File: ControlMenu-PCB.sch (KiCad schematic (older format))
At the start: 6 parts, among them J1 Conn_01x08, J2 Conn_01x04

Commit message: autosync
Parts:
- 100s1, 10s1, 1s1, Enter1: footprint RobsFoots:PB86-A-FP -> AA-ROB-FULL:PB86-A-FP; symbol robsym1:PB-86A -> AA_ROB:PB-86A-robsym1
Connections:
- wire segments 51 -> 52
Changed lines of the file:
@@
 $EndDescr
 $Comp
-L robsym1:PB-86A 100s1
+L AA_ROB:PB-86A-robsym1 100s1
 U 1 1 5FEB2BAB
 P 4300 3350
 F 0 "100s1" H 4550 4225 50  0000 C CNN
 F 1 "PB-86A" H 4550 4134 50  0000 C CNN
-F 2 "RobsFoots:PB86-A-FP" H 4300 3350 50  0001 C CNN
+F 2 "AA-ROB-FULL:PB86-A-FP" H 4300 3350 50  0001 C CNN
 F 3 "" H 4300 3350 50  0001 C CNN
 	1    4300 3350
@@
 $EndComp
 $Comp
-L robsym1:PB-86A 10s1
+L AA_ROB:PB-86A-robsym1 10s1
 U 1 1 5FEB3BFC
 P 5600 3350
 F 0 "10s1" H 5850 4225 50  0000 C CNN
 F 1 "PB-86A" H 5850 4134 50  0000 C CNN
-F 2 "RobsFoots:PB86-A-FP" H 5600 3350 50  0001 C CNN
+F 2 "AA-ROB-FULL:PB86-A-FP" H 5600 3350 50  0001 C CNN
 F 3 "" H 5600 3350 50  0001 C CNN
 	1    5600 3350
@@
 $EndComp
 $Comp
-L robsym1:PB-86A Enter1
+L AA_ROB:PB-86A-robsym1 Enter1
 U 1 1 5FEB56A3
 P 8300 3350
 F 0 "Enter1" H 8550 4225 50  0000 C CNN
 F 1 "PB-86A" H 8550 4134 50  0000 C CNN
-F 2 "RobsFoots:PB86-A-FP" H 8300 3350 50  0001 C CNN
+F 2 "AA-ROB-FULL:PB86-A-FP" H 8300 3350 50  0001 C CNN
 F 3 "" H 8300 3350 50  0001 C CNN
 	1    8300 3350
@@
 	3400 2850 3400 3400
 Wire Wire Line
-	9450 3400 9450 2600
+	9450 3400 9450 2800
 Wire Wire Line
 	9450 2600 9800 2600
@@
 	4000 2850 3900 2850
 $Comp
-L robsym1:PB-86A 1s1
+L AA_ROB:PB-86A-robsym1 1s1
 U 1 1 5FEB4A66
 P 6900 3350
 F 0 "1s1" H 7150 4225 50  0000 C CNN
 F 1 "PB-86A" H 7150 4134 50  0000 C CNN
-F 2 "RobsFoots:PB86-A-FP" H 6900 3350 50  0001 C CNN
+F 2 "AA-ROB-FULL:PB86-A-FP" H 6900 3350 50  0001 C CNN
 F 3 "" H 6900 3350 50  0001 C CNN
 	1    6900 3350
 	1    0    0    -1
 $EndComp
-Connection ~ 9250 2800
-Wire Wire Line
-	9250 2800 9250 2300
 Wire Wire Line
 	5300 2850 5300 2800
@@
 Wire Wire Line
 	8000 2800 9250 2800
-Wire Wire Line
-	3900 2150 2400 2150
 Connection ~ 5050 2800
 Wire Wire Line
-	3900 2800 3900 2150
-Wire Wire Line
 	3900 2850 3900 2800
-Connection ~ 3900 2800
 Wire Wire Line
 	3900 2800 5050 2800
 Text Notes 7150 6850 0    50   ~ 0
 Version V0.1.1
+Wire Wire Line
+	9250 2150 9250 2300
+Wire Wire Line
+	2400 2150 9250 2150
+Wire Wire Line
+	9250 2800 9450 2800
+Connection ~ 9250 2800
+Connection ~ 9450 2800
+Wire Wire Line
+	9450 2800 9450 2600
 $EndSCHEMATC

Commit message: 5V to Ground Fixes
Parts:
- 100s1, 10s1, 1s1, Enter1: symbol AA_ROB:PB-86A-robsym1 -> AA-ROBSCH:PB-86A
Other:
- note added: "Version V0.1.2"
- note removed: "Version V0.1.1"
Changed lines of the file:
@@
 $EndDescr
 $Comp
-L AA_ROB:PB-86A-robsym1 100s1
+L AA-ROBSCH:PB-86A 100s1
 U 1 1 5FEB2BAB
 P 4300 3350
@@
 $EndComp
 $Comp
-L AA_ROB:PB-86A-robsym1 10s1
+L AA-ROBSCH:PB-86A 10s1
 U 1 1 5FEB3BFC
 P 5600 3350
@@
 $EndComp
 $Comp
-L AA_ROB:PB-86A-robsym1 Enter1
+L AA-ROBSCH:PB-86A Enter1
 U 1 1 5FEB56A3
 P 8300 3350
@@
 Wire Wire Line
 	9250 2850 9250 2800
-Wire Wire Line
-	9250 2300 9800 2300
 $Comp
 L Connector_Generic:Conn_01x04 J2
@@
 Text Notes 9700 2600 0    50   ~ 0
 GND
-Text Label 9250 2450 0    50   ~ 0
-5V
 Text Label 9450 2400 0    50   ~ 0
 SDA
@@
 	4000 2850 3900 2850
 $Comp
-L AA_ROB:PB-86A-robsym1 1s1
+L AA-ROBSCH:PB-86A 1s1
 U 1 1 5FEB4A66
 P 6900 3350
@@
 	3900 2800 5050 2800
 Text Notes 7150 6850 0    50   ~ 0
-Version V0.1.1
-Wire Wire Line
-	9250 2150 9250 2300
-Wire Wire Line
-	2400 2150 9250 2150
+Version V0.1.2
 Wire Wire Line
 	9250 2800 9450 2800
@@
 Wire Wire Line
 	9450 2800 9450 2600
+Wire Wire Line
+	2400 2150 9800 2150
+Wire Wire Line
+	9800 2150 9800 2300
 $EndSCHEMATC

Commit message: RC
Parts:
- 100s1, 10s1, 1s1, Enter1: symbol AA-ROBSCH:PB-86A -> AA-ROBSCH:PB-86A-robsym1
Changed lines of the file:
@@
 $EndDescr
 $Comp
-L AA-ROBSCH:PB-86A 100s1
+L AA-ROBSCH:PB-86A-robsym1 100s1
 U 1 1 5FEB2BAB
 P 4300 3350
@@
 $EndComp
 $Comp
-L AA-ROBSCH:PB-86A 10s1
+L AA-ROBSCH:PB-86A-robsym1 10s1
 U 1 1 5FEB3BFC
 P 5600 3350
@@
 $EndComp
 $Comp
-L AA-ROBSCH:PB-86A Enter1
+L AA-ROBSCH:PB-86A-robsym1 Enter1
 U 1 1 5FEB56A3
 P 8300 3350
@@
 	4000 2850 3900 2850
 $Comp
-L AA-ROBSCH:PB-86A 1s1
+L AA-ROBSCH:PB-86A-robsym1 1s1
 U 1 1 5FEB4A66
 P 6900 3350

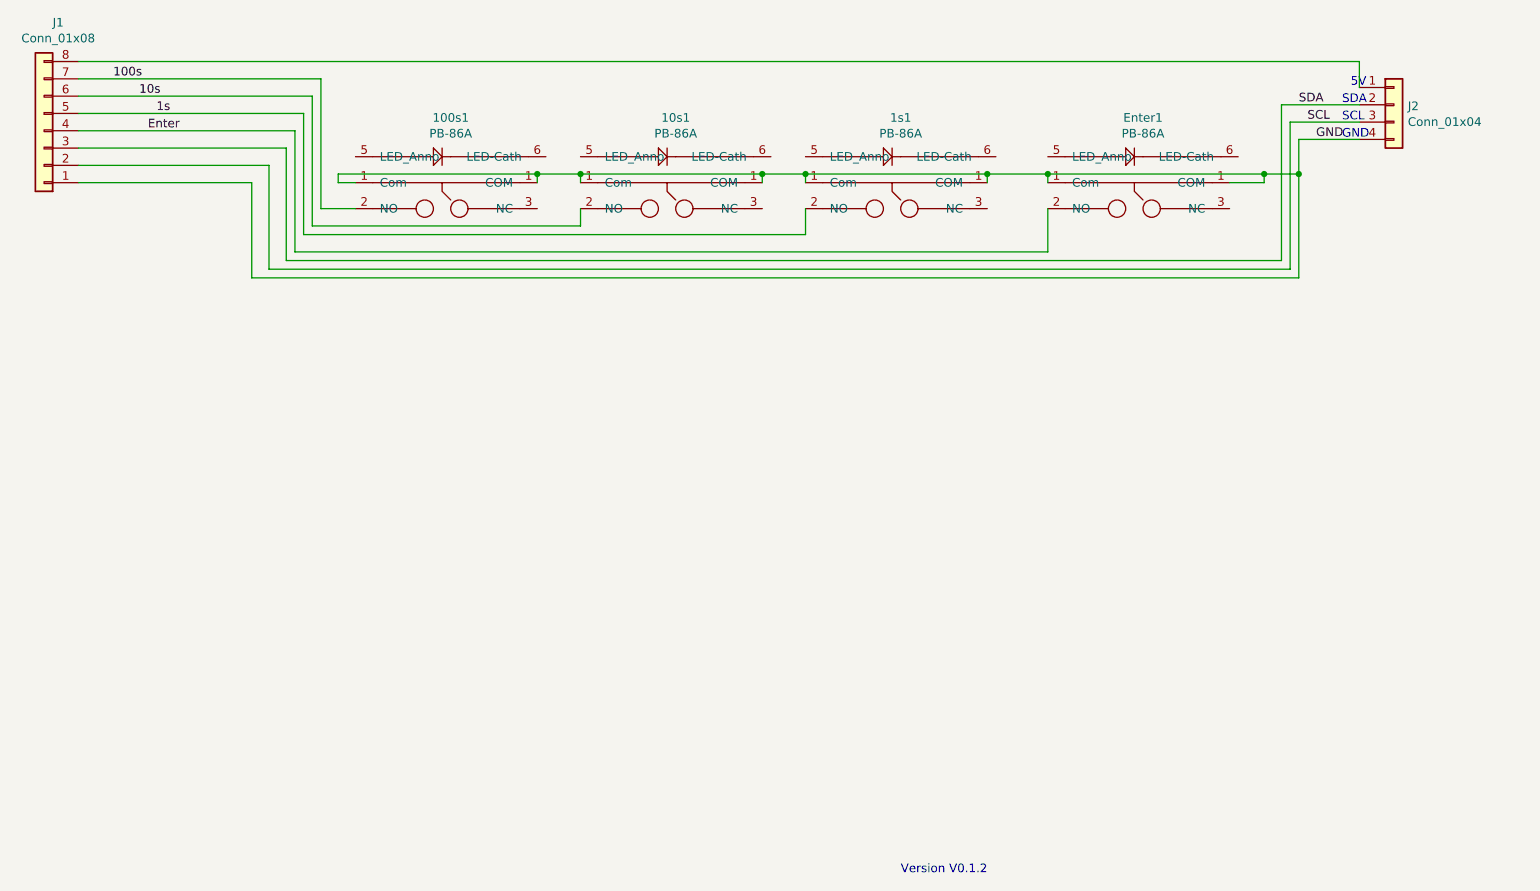
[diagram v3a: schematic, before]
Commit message: Screen mount cutout reduced, I2C re-ordered.
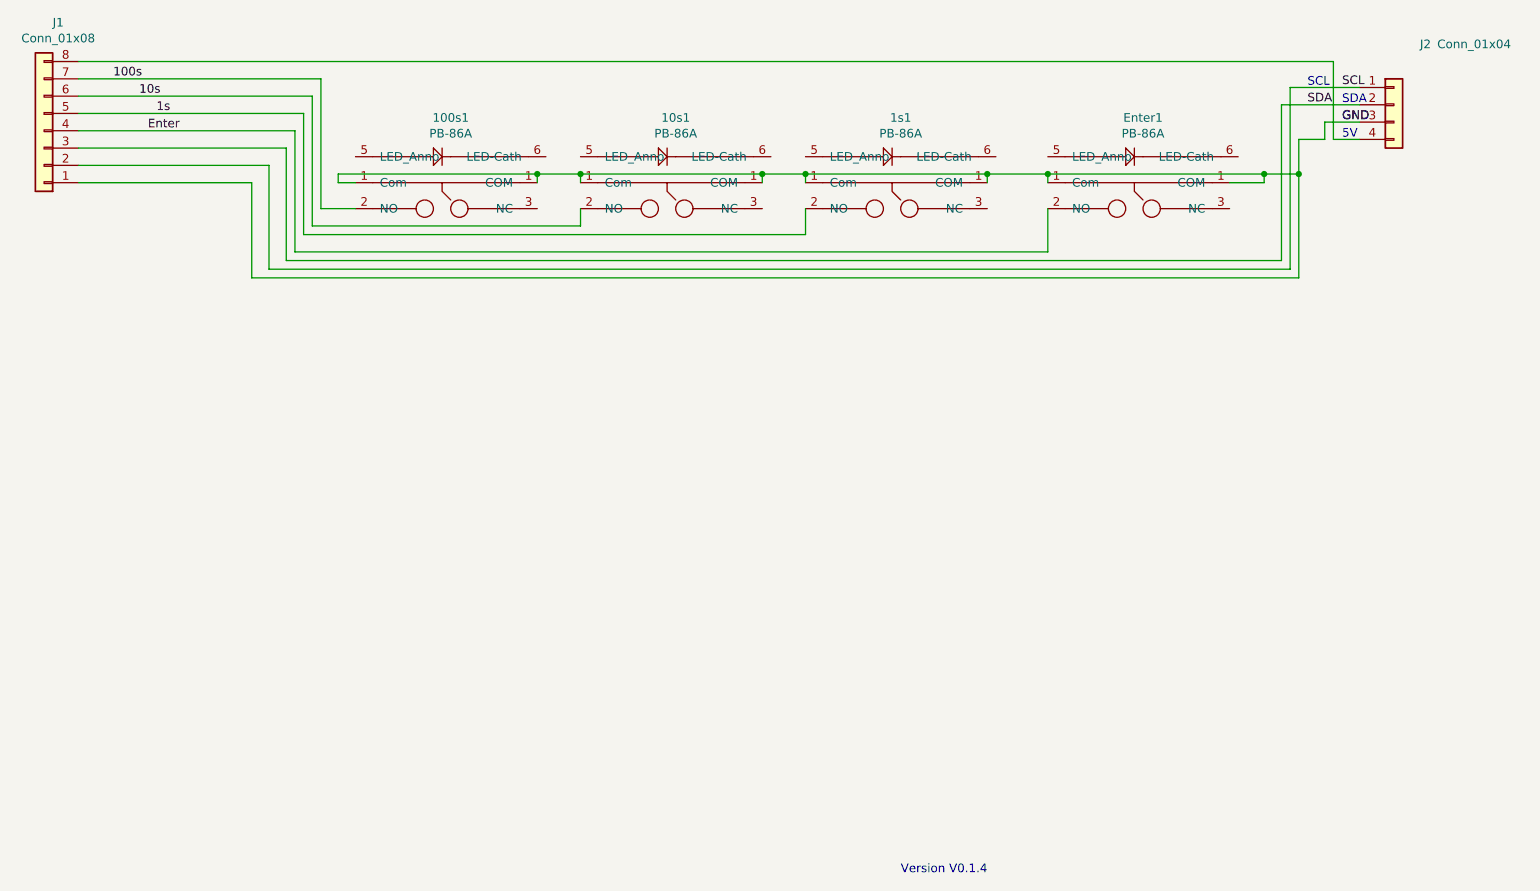
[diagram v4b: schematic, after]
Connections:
- net GND: now also J2.3 (Pin_3); no longer J2.4 (Pin_4)
- net SCL: now also J2.1 (Pin_1); no longer J2.3 (Pin_3)
- net at J1.8 (Pin_8): now also J2.4 (Pin_4); no longer J2.1 (Pin_1)
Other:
- note added: "Version V0.1.4\n"
- note removed: "Version V0.1.2"
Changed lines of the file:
@@
 	3500 3350 9400 3350
-Wire Wire Line
-	9400 3350 9400 2500
 Wire Wire Line
 	2400 2850 3400 2850
@@
 Wire Wire Line
 	9450 3400 9450 2800
-Wire Wire Line
-	9450 2600 9800 2600
 Wire Wire Line
 	9050 2850 9250 2850
@@
 U 1 1 5FEC2557
 P 10000 2400
-F 0 "J2" H 10080 2392 50  0000 L CNN
-F 1 "Conn_01x04" H 10080 2301 50  0000 L CNN
+F 0 "J2" H 10150 2750 50  0000 L CNN
+F 1 "Conn_01x04" H 10250 2750 50  0000 L CNN
 F 2 "Connector_PinHeader_2.54mm:PinHeader_1x04_P2.54mm_Horizontal" H 10000 2400 50  0001 C CNN
 F 3 "~" H 10000 2400 50  0001 C CNN
@@
 	1    0    0    -1
 $EndComp
-Wire Wire Line
-	9800 2500 9400 2500
-Text Notes 9750 2300 0    50   ~ 0
+Text Notes 9700 2600 0    50   ~ 0
 5V
 Wire Wire Line
@@
 Text Notes 9700 2400 0    50   ~ 0
 SDA
+Text Notes 9500 2300 0    50   ~ 0
+SCL
 Text Notes 9700 2500 0    50   ~ 0
+GND
+Text Label 9500 2400 0    50   ~ 0
+SDA
+Text Label 9700 2300 0    50   ~ 0
 SCL
-Text Notes 9700 2600 0    50   ~ 0
-GND
-Text Label 9450 2400 0    50   ~ 0
-SDA
-Text Label 9500 2500 0    50   ~ 0
-SCL
-Text Label 9550 2600 0    50   ~ 0
+Text Label 9700 2500 0    50   ~ 0
 GND
 Text Label 2600 2250 0    50   ~ 0
@@
 	3900 2800 5050 2800
 Text Notes 7150 6850 0    50   ~ 0
-Version V0.1.2
+Version V0.1.4\n
 Wire Wire Line
 	9250 2800 9450 2800
@@
 	9450 2800 9450 2600
 Wire Wire Line
-	2400 2150 9800 2150
+	2400 2150 9650 2150
 Wire Wire Line
-	9800 2150 9800 2300
+	9400 2300 9800 2300
+Wire Wire Line
+	9400 2300 9400 3350
+Wire Wire Line
+	9650 2150 9650 2600
+Wire Wire Line
+	9650 2600 9800 2600
+Wire Wire Line
+	9450 2600 9600 2600
+Wire Wire Line
+	9600 2600 9600 2500
+Wire Wire Line
+	9600 2500 9800 2500
 $EndSCHEMATC
